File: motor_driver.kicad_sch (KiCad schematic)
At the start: 16 parts, among them M1 Motor_DC, M2 Motor_DC, M3 Motor_DC, M4 Motor_DC, U3 DRV8833PWP, U5 DRV8833PWP

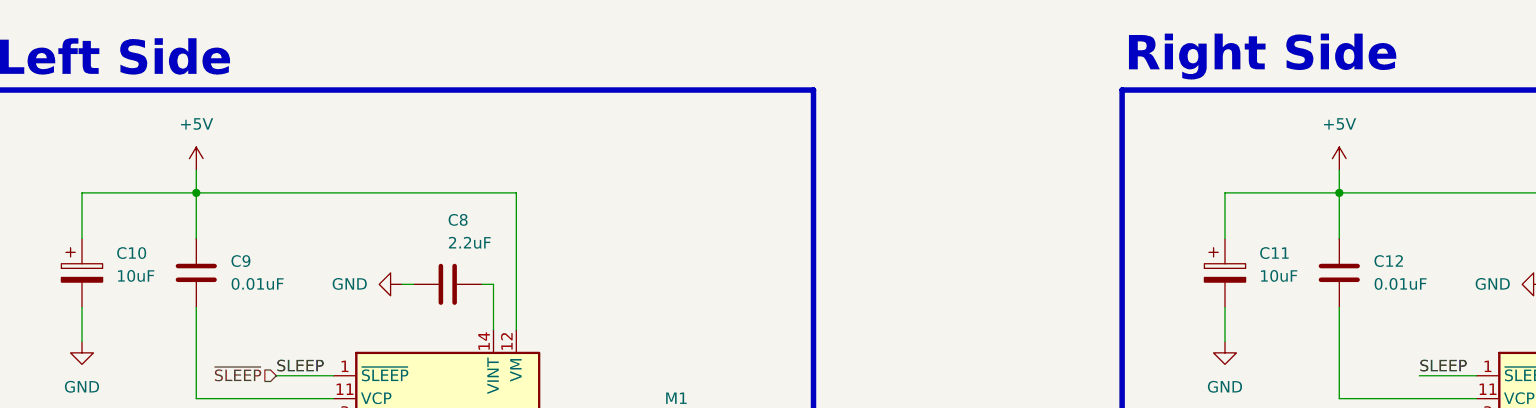
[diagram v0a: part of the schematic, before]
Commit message: update schematic
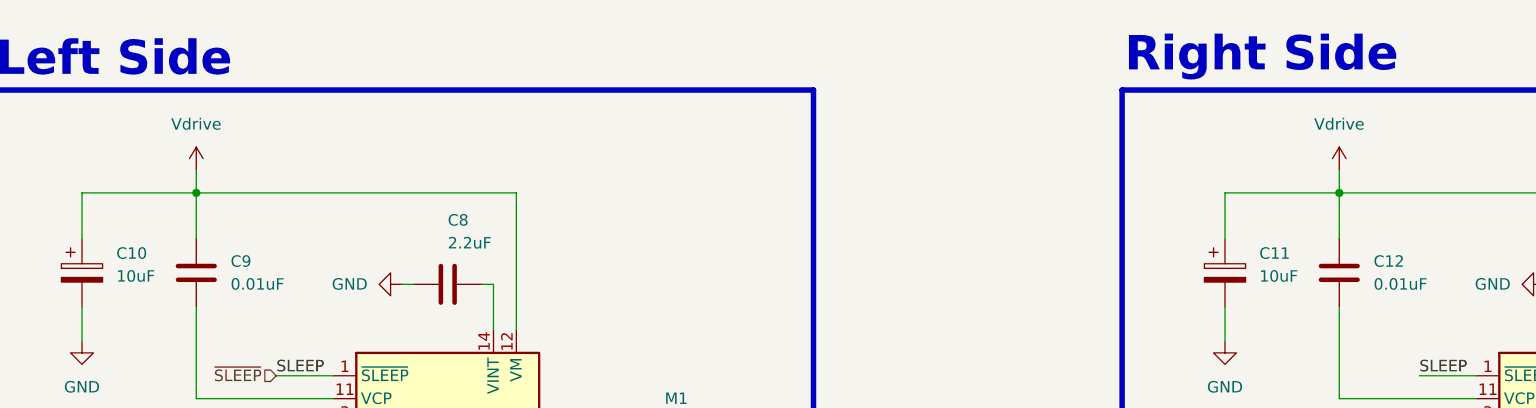
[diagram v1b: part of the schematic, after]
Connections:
- net +5V renamed Vdrive

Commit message: improve design
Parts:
- removed C11: 10uF, symbol Device:C_Polarized
- removed C12: 0.01uF, symbol Device:C
- removed C13: 2.2uF, symbol Device:C
- removed M3, M4: Motor_DC, symbol Motor:Motor_DC
- removed R11, R12: 200m, symbol Device:R
- removed U5: DRV8833PWP, Package_SO:HTSSOP-16-1EP_4.4x5mm_P0.65mm_EP3.4x5mm_Mask2.46x2.31mm_ThermalVias, symbol Driver_Motor:DRV8833PWP
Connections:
- net LIN1 renamed AIN1
- net AIN1: no longer U3.9 (BIN1)
- net LIN2 renamed AIN2
- net AIN2: no longer U3.10 (BIN2)
- new net BIN1: U3.9 (BIN1)
- new net BIN2: U3.10 (BIN2)
- no-connect marks 2 -> 1
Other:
- note removed: "Left Side"
- note removed: "Right Side"
- title: (none) -> Dropbot
- moved on the sheet: C10, C8, C9, M1, M2, R10, R9, U3

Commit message: moving on routing
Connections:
- net Vdrive renamed +6V
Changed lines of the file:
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@@
-	)
-	(symbol
-		(lib_id "power:Vdrive")
-		(at 115.57 74.93 0)
-		(unit 1)
-		(body_style 1)
-		(exclude_from_sim no)
-		(in_bom yes)
-		(on_board yes)
-		(in_pos_files yes)
-		(dnp no)
-		(fields_autoplaced yes)
-		(property "Reference" "#PWR027"
-			(at 115.57 78.74 0)
-			(hide yes)
-			(show_name no)
-			(do_not_autoplace no)
-			(effects
-				(font
-					(size 1.27 1.27)
-				)
-			)
-		)
-		(property "Value" "Vdrive"
-			(at 115.57 69.85 0)
-			(show_name no)
-			(do_not_autoplace no)
-			(effects
-				(font
-					(size 1.27 1.27)
-				)
-			)
-		)
-		(property "Footprint" ""
-			(at 115.57 74.93 0)
-			(hide yes)
-			(show_name no)
-			(do_not_autoplace no)
-			(effects
-				(font
-					(size 1.27 1.27)
-				)
-			)
-		)
-		(property "Datasheet" ""
-			(at 115.57 74.93 0)
-			(hide yes)
-			(show_name no)
-			(do_not_autoplace no)
-			(effects
-				(font
-					(size 1.27 1.27)
-				)
-			)
-		)
-		(property "Description" "Power symbol creates a global label with name \"Vdrive\""
-			(at 115.57 74.93 0)
-			(hide yes)
-			(show_name no)
-			(do_not_autoplace no)
-			(effects
-				(font
-					(size 1.27 1.27)
-				)
-			)
-		)
-		(pin "1"
-		)
-		(instances
-			(project "rover-circuit"
-				(path "/0461baee-3b25-4e1a-a5c1-d76b4b99c66c/6fd78103-703b-49c2-b552-015594035fd1"
-					(reference "#PWR027")
-					(unit 1)
-				)
-			)
-		)
 	)
 	(symbol
@@
 					(unit 1)
 				)
+			)
+		)
+	)
+	(symbol
+		(lib_id "power:+6V")
+		(at 115.57 74.93 0)
+		(unit 1)
+		(body_style 1)
+		(exclude_from_sim no)
+		(in_bom yes)
+		(on_board yes)
+		(in_pos_files yes)
+		(dnp no)
+		(fields_autoplaced yes)
+		(property "Reference" "#PWR021"
+			(at 115.57 78.74 0)
+			(hide yes)
+			(show_name no)
+			(do_not_autoplace no)
+			(effects
+				(font
+					(size 1.27 1.27)
+				)
+			)
+		)
+		(property "Value" "+6V"
+			(at 115.57 69.85 0)
+			(show_name no)
+			(do_not_autoplace no)
+			(effects
+				(font
+					(size 1.27 1.27)
+				)
+			)
+		)
+		(property "Footprint" ""
+			(at 115.57 74.93 0)
+			(hide yes)
+			(show_name no)
+			(do_not_autoplace no)
+			(effects
+				(font
+					(size 1.27 1.27)
+				)
+			)
+		)
+		(property "Datasheet" ""
+			(at 115.57 74.93 0)
+			(hide yes)
+			(show_name no)
+			(do_not_autoplace no)
+			(effects
+				(font
+					(size 1.27 1.27)
+				)
+			)
+		)
+		(property "Description" "Power symbol creates a global label with name \"+6V\""
+			(at 115.57 74.93 0)
+			(hide yes)
+			(show_name no)
+			(do_not_autoplace no)
+			(effects
+				(font
+					(size 1.27 1.27)
+				)
+			)
+		)
+		(pin "1"
+		)
+		(instances
+			(project "rover-circuit"
+				(path "/0461baee-3b25-4e1a-a5c1-d76b4b99c66c/6fd78103-703b-49c2-b552-015594035fd1"
+					(reference "#PWR021")
+					(unit 1)
+				)

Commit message: update PCB
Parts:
- M1, M2: footprint (none) -> Connector_JST:JST_PH_B2B-PH-SM4-TB_1x02-1MP_P2.00mm_Vertical
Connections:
- net at U3.2 (AOUT1): now also M1.2 (-); no longer M1.1 (+)
- net at U3.4 (AOUT2): now also M1.1 (+); no longer M1.2 (-)
- net at U3.5 (BOUT2): now also M2.2 (-); no longer M2.1 (+)
- net at U3.7 (BOUT1): now also M2.1 (+); no longer M2.2 (-)
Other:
- moved on the sheet: M1, M2
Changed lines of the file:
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@@
 	(symbol
 		(lib_id "Motor:Motor_DC")
-		(at 166.37 120.65 90)
-		(mirror x)
+		(at 168.91 120.65 270)
 		(unit 1)
 		(body_style 1)
@@
 		(dnp no)
 		(property "Reference" "M2"
-			(at 168.91 128.27 90)
+			(at 166.37 128.27 90)
 			(show_name no)
 			(do_not_autoplace no)
@@
 		)
 		(property "Value" "Motor_DC"
-			(at 168.91 125.73 90)
-			(show_name no)
-			(do_not_autoplace no)
-			(effects
-				(font
-					(size 1.27 1.27)
-				)
-			)
-		)
-		(property "Footprint" ""
-			(at 168.656 120.65 0)
-			(hide yes)
-			(show_name no)
-			(do_not_autoplace no)
-			(effects
-				(font
-					(size 1.27 1.27)
-				)
-			)
-		)
-		(property "Datasheet" ""
-			(at 168.656 120.65 0)
+			(at 166.37 125.73 90)
+			(show_name no)
+			(do_not_autoplace no)
+			(effects
+				(font
+					(size 1.27 1.27)
+				)
+			)
+		)
+		(property "Footprint" "Connector_JST:JST_PH_B2B-PH-SM4-TB_1x02-1MP_P2.00mm_Vertical"
+			(at 166.624 120.65 0)
+			(hide yes)
+			(show_name no)
+			(do_not_autoplace no)
+			(effects
+				(font
+					(size 1.27 1.27)
+				)
+			)
+		)
+		(property "Datasheet" ""
+			(at 166.624 120.65 0)
 			(hide yes)
 			(show_name no)
@@
 		)
 		(property "Description" "DC Motor"
-			(at 166.37 120.65 0)
+			(at 168.91 120.65 0)
 			(hide yes)
 			(show_name no)
@@
 	(symbol
 		(lib_id "Motor:Motor_DC")
-		(at 166.37 107.95 90)
+		(at 168.91 107.95 270)
 		(unit 1)
 		(body_style 1)
@@
 		(fields_autoplaced yes)
 		(property "Reference" "M1"
-			(at 168.91 100.33 90)
+			(at 166.37 100.33 90)
 			(show_name no)
 			(do_not_autoplace no)
@@
 		)
 		(property "Value" "Motor_DC"
-			(at 168.91 102.87 90)
-			(show_name no)
-			(do_not_autoplace no)
-			(effects
-				(font
-					(size 1.27 1.27)
-				)
-			)
-		)
-		(property "Footprint" ""
-			(at 168.656 107.95 0)
-			(hide yes)
-			(show_name no)
-			(do_not_autoplace no)
-			(effects
-				(font
-					(size 1.27 1.27)
-				)
-			)
-		)
-		(property "Datasheet" ""
-			(at 168.656 107.95 0)
+			(at 166.37 102.87 90)
+			(show_name no)
+			(do_not_autoplace no)
+			(effects
+				(font
+					(size 1.27 1.27)
+				)
+			)
+		)
+		(property "Footprint" "Connector_JST:JST_PH_B2B-PH-SM4-TB_1x02-1MP_P2.00mm_Vertical"
+			(at 166.624 107.95 0)
+			(hide yes)
+			(show_name no)
+			(do_not_autoplace no)
+			(effects
+				(font
+					(size 1.27 1.27)
+				)
+			)
+		)
+		(property "Datasheet" ""
+			(at 166.624 107.95 0)
 			(hide yes)
 			(show_name no)
@@
 		)
 		(property "Description" "DC Motor"
-			(at 166.37 107.95 0)
-			(hide yes)
-			(show_name no)
+			(at 168.91 107.95 0)
+			(hide yes)
+			(show_name no)

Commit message: some progress
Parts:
- M1, M2: footprint Connector_JST:JST_PH_B2B-PH-SM4-TB_1x02-1MP_P2.00mm_Vertical -> Connector_JST:JST_PH_S2B-PH-SM4-TB_1x02-1MP_P2.00mm_Horizontal
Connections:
- net at U3.2 (AOUT1): now also M1.1 (+); no longer M1.2 (-)
- net at U3.4 (AOUT2): now also M1.2 (-); no longer M1.1 (+)
- net at U3.5 (BOUT2): now also M2.1 (+); no longer M2.2 (-)
- net at U3.7 (BOUT1): now also M2.2 (-); no longer M2.1 (+)
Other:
- moved on the sheet: M1, M2
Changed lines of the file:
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@@
 	(symbol
 		(lib_id "Motor:Motor_DC")
-		(at 168.91 120.65 270)
+		(at 166.37 120.65 90)
+		(mirror x)
 		(unit 1)
 		(body_style 1)
@@
 		(dnp no)
 		(property "Reference" "M2"
-			(at 166.37 128.27 90)
+			(at 168.91 128.27 90)
 			(show_name no)
 			(do_not_autoplace no)
@@
 		)
 		(property "Value" "Motor_DC"
-			(at 166.37 125.73 90)
-			(show_name no)
-			(do_not_autoplace no)
-			(effects
-				(font
-					(size 1.27 1.27)
-				)
-			)
-		)
-		(property "Footprint" "Connector_JST:JST_PH_B2B-PH-SM4-TB_1x02-1MP_P2.00mm_Vertical"
-			(at 166.624 120.65 0)
-			(hide yes)
-			(show_name no)
-			(do_not_autoplace no)
-			(effects
-				(font
-					(size 1.27 1.27)
-				)
-			)
-		)
-		(property "Datasheet" ""
-			(at 166.624 120.65 0)
+			(at 168.91 125.73 90)
+			(show_name no)
+			(do_not_autoplace no)
+			(effects
+				(font
+					(size 1.27 1.27)
+				)
+			)
+		)
+		(property "Footprint" "Connector_JST:JST_PH_S2B-PH-SM4-TB_1x02-1MP_P2.00mm_Horizontal"
+			(at 168.656 120.65 0)
+			(hide yes)
+			(show_name no)
+			(do_not_autoplace no)
+			(effects
+				(font
+					(size 1.27 1.27)
+				)
+			)
+		)
+		(property "Datasheet" ""
+			(at 168.656 120.65 0)
 			(hide yes)
 			(show_name no)
@@
 		)
 		(property "Description" "DC Motor"
-			(at 168.91 120.65 0)
+			(at 166.37 120.65 0)
 			(hide yes)
 			(show_name no)
@@
 	(symbol
 		(lib_id "Motor:Motor_DC")
-		(at 168.91 107.95 270)
+		(at 166.37 107.95 90)
 		(unit 1)
 		(body_style 1)
@@
 		(fields_autoplaced yes)
 		(property "Reference" "M1"
-			(at 166.37 100.33 90)
+			(at 168.91 100.33 90)
 			(show_name no)
 			(do_not_autoplace no)
@@
 		)
 		(property "Value" "Motor_DC"
-			(at 166.37 102.87 90)
-			(show_name no)
-			(do_not_autoplace no)
-			(effects
-				(font
-					(size 1.27 1.27)
-				)
-			)
-		)
-		(property "Footprint" "Connector_JST:JST_PH_B2B-PH-SM4-TB_1x02-1MP_P2.00mm_Vertical"
-			(at 166.624 107.95 0)
-			(hide yes)
-			(show_name no)
-			(do_not_autoplace no)
-			(effects
-				(font
-					(size 1.27 1.27)
-				)
-			)
-		)
-		(property "Datasheet" ""
-			(at 166.624 107.95 0)
+			(at 168.91 102.87 90)
+			(show_name no)
+			(do_not_autoplace no)
+			(effects
+				(font
+					(size 1.27 1.27)
+				)
+			)
+		)
+		(property "Footprint" "Connector_JST:JST_PH_S2B-PH-SM4-TB_1x02-1MP_P2.00mm_Horizontal"
+			(at 168.656 107.95 0)
+			(hide yes)
+			(show_name no)
+			(do_not_autoplace no)
+			(effects
+				(font
+					(size 1.27 1.27)
+				)
+			)
+		)
+		(property "Datasheet" ""
+			(at 168.656 107.95 0)
 			(hide yes)
 			(show_name no)
@@
 		)
 		(property "Description" "DC Motor"
-			(at 168.91 107.95 0)
-			(hide yes)
-			(show_name no)
+			(at 166.37 107.95 0)
+			(hide yes)
+			(show_name no)

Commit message: more on routing and schematic
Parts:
- added C11: 10uF, Capacitor_SMD:C_0805_2012Metric, symbol Device:C
- C10: value 10uF -> 100uF; footprint (none) -> Capacitor_SMD:CP_Elec_6.3x5.4
- C8: footprint (none) -> Capacitor_SMD:C_0603_1608Metric
- C9: value 0.01uF -> 10nF; footprint (none) -> Capacitor_SMD:C_0603_1608Metric
- R10, R9: footprint (none) -> Resistor_SMD:R_1206_3216Metric
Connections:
- net +6V: now also C11.1
- net GND: now also C11.2
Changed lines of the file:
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@@
+		(color 0 0 0 0)
+	)
+	(junction
+		(at 151.13 77.47)
+		(diameter 0)
 		(color 0 0 0 0)
 	)
@@
 	(wire
 		(pts
+			(xy 151.13 77.47) (xy 158.75 77.47)
+		)
+		(stroke
+			(width 0)
+			(type default)
+		)
+	)
+	(wire
+		(pts
 			(xy 156.21 113.03) (xy 175.26 113.03)
 		)
@@
 	(wire
 		(pts
+			(xy 158.75 87.63) (xy 158.75 88.9)
+		)
+		(stroke
+			(width 0)
+			(type default)
+		)
+	)
+	(wire
+		(pts
 			(xy 115.57 74.93) (xy 115.57 77.47)
 		)
@@
 		(pts
 			(xy 160.02 107.95) (xy 160.02 110.49)
+		)
+		(stroke
+			(width 0)
+			(type default)
+		)
+	)
+	(wire
+		(pts
+			(xy 158.75 77.47) (xy 158.75 80.01)
 		)
 		(stroke
@@
 	)
 	(symbol
+		(lib_id "Device:C")
+		(at 158.75 83.82 0)
+		(unit 1)
+		(body_style 1)
+		(exclude_from_sim no)
+		(in_bom yes)
+		(on_board yes)
+		(in_pos_files yes)
+		(dnp no)
+		(fields_autoplaced yes)
+		(property "Reference" "C11"
+			(at 162.56 82.5499 0)
+			(show_name no)
+			(do_not_autoplace no)
+			(effects
+				(font
+					(size 1.27 1.27)
+				)
+				(justify left)
+			)
+		)
+		(property "Value" "10uF"
+			(at 162.56 85.0899 0)
+			(show_name no)
+			(do_not_autoplace no)
+			(effects
+				(font
+					(size 1.27 1.27)
+				)
+				(justify left)
+			)
+		)
+		(property "Footprint" "Capacitor_SMD:C_0805_2012Metric"
+			(at 159.7152 87.63 0)
+			(hide yes)
+			(show_name no)
+			(do_not_autoplace no)
+			(effects
+				(font
+					(size 1.27 1.27)
+				)
+			)
+		)
+		(property "Datasheet" ""
+			(at 158.75 83.82 0)
+			(hide yes)
+			(show_name no)
+			(do_not_autoplace no)
+			(effects
+				(font
+					(size 1.27 1.27)
+				)
+			)
+		)
+		(property "Description" "Unpolarized capacitor"
+			(at 158.75 83.82 0)
+			(hide yes)
+			(show_name no)
+			(do_not_autoplace no)
+			(effects
+				(font
+					(size 1.27 1.27)
+				)
+			)
+		)
+		(pin "1"
+		)
+		(pin "2"
+		)
+		(instances
+			(project "rover-circuit"
+				(path "/0461baee-3b25-4e1a-a5c1-d76b4b99c66c/6fd78103-703b-49c2-b552-015594035fd1"
+					(reference "C11")
+					(unit 1)
+				)
+			)
+		)
+	)
+	(symbol
 		(lib_id "power:GND")
 		(at 102.87 93.98 0)
@@
 			)
 		)
-		(property "Value" "10uF"
+		(property "Value" "100uF"
 			(at 106.68 86.7409 0)
 			(show_name no)
@@
 			)
 		)
-		(property "Footprint" ""
+		(property "Footprint" "Capacitor_SMD:CP_Elec_6.3x5.4"
 			(at 103.8352 90.17 0)
 			(hide yes)
@@
 			)
 		)
-		(property "Value" "0.01uF"
+		(property "Value" "10nF"
 			(at 119.38 87.6299 0)
 			(show_name no)
@@
 			)
 		)
-		(property "Footprint" ""
+		(property "Footprint" "Capacitor_SMD:C_0603_1608Metric"
 			(at 116.5352 90.17 0)
 			(hide yes)
@@
 	)
 	(symbol
+		(lib_id "power:GND")
+		(at 158.75 88.9 0)
+		(unit 1)
+		(body_style 1)
+		(exclude_from_sim no)
+		(in_bom yes)
+		(on_board yes)
+		(in_pos_files yes)
+		(dnp no)
+		(fields_autoplaced yes)
+		(property "Reference" "#PWR027"
+			(at 158.75 95.25 0)
+			(hide yes)
+			(show_name no)
+			(do_not_autoplace no)
+			(effects
+				(font
+					(size 1.27 1.27)
+				)
+			)
+		)
+		(property "Value" "GND"
+			(at 158.75 93.98 0)
+			(show_name no)
+			(do_not_autoplace no)
+			(effects
+				(font
+					(size 1.27 1.27)
+				)
+			)
+		)
+		(property "Footprint" ""
+			(at 158.75 88.9 0)
+			(hide yes)
+			(show_name no)
+			(do_not_autoplace no)
+			(effects
+				(font
+					(size 1.27 1.27)
+				)
+			)
+		)
+		(property "Datasheet" ""
+			(at 158.75 88.9 0)
+			(hide yes)
+			(show_name no)
+			(do_not_autoplace no)
+			(effects
+				(font
+					(size 1.27 1.27)
+				)
+			)
+		)
+		(property "Description" "Power symbol creates a global label with name \"GND\" , ground"
+			(at 158.75 88.9 0)
+			(hide yes)
+			(show_name no)
+			(do_not_autoplace no)
+			(effects
+				(font
+					(size 1.27 1.27)
+				)
+			)
+		)
+		(pin "1"
+		)
+		(instances
+			(project "rover-circuit"
+				(path "/0461baee-3b25-4e1a-a5c1-d76b4b99c66c/6fd78103-703b-49c2-b552-015594035fd1"
+					(reference "#PWR027")
+					(unit 1)
+				)
+			)
+		)
+	)
+	(symbol
 		(lib_id "Motor:Motor_DC")
 		(at 166.37 120.65 90)
@@
 			)
 		)
-		(property "Footprint" ""
+		(property "Footprint" "Resistor_SMD:R_1206_3216Metric"
 			(at 116.078 110.49 90)
 			(hide yes)
@@
 			)
 		)
-		(property "Footprint" ""
+		(property "Footprint" "Resistor_SMD:R_1206_3216Metric"
 			(at 104.648 110.49 90)
 			(hide yes)
@@
 			)
 		)
-		(property "Footprint" ""
+		(property "Footprint" "Capacitor_SMD:C_0603_1608Metric"
 			(at 139.7 86.6648 0)
 			(hide yes)

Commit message: complete routing and validated ERC/DRC
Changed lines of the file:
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@@
-		)
-	)
-	(label "SLEEP"
-		(at 124.46 97.79 0)
-		(effects
-			(font
-				(size 1.27 1.27)
-			)
-			(justify left bottom)
 		)
 	)
